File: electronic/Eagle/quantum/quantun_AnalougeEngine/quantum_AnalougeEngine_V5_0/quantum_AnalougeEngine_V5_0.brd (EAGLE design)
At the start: 200 x 80 mm, 198 parts, among them IC1 OP275, IC10 STM32F767ZIT6, IC11 AD7606BSTZ, IC12 ESDA6V1BC6, IC2 DAC084S085CIMM_NOPB, IC3 DAC084S085CIMM_NOPB, IC4 OP275, IC5 OP275, IC6 LAN8742A-CZ-TR, IC7 TL072, IC8 OP275, IC9 TL072, J1 GWLEX-SMT-S988G_Y, K1 K1, K2 K2, K3 K3, K4 K4, K5 K5, K6 K6, K7 K7, K8 K8, T1 H1102NL, U12 ULN2003, U4 THAT1240, U6 THAT1240, U7 THAT1240, U8 THAT1240

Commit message: progress Analog Engine V_5_0
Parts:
- removed ANALOGVOLT, DIG_VOLT: 90814-0204, electro_mechanical:MOLEX_90814-0204
- removed LED10, LED11, LED9: LED_BLUE_SMD, C_Sager_Bibliothek:WL-SMCW_0603
- added +12V_OK, +15V_OK, +3V3_OK, +5V_OK, -15V_OK: LED_GREEN_SMD, passive components:WL-SMCW_0603
- added ANALOG_VOLT, DIGITAL_VOLT, DISPLAY: 90814-0204, electro_mechanical:MOLEX_90814-0204
- added C100: 30 pF, passive components:C0603
- added C101: 4.7 uF, passive components:C1206
- added C102, C91, C99: 10 uF, passive components:C1206
- added C103, C95, C96, C97, C98: 100nF, C_Sager_Bibliothek:C0603
- added C65, C66: 2.7 pF, passive components:C0603
- added C69, C70: 4.3 pF, passive components:C0603
- added C71, C72: 2.2 uF, passive components:C1206
- added C73, C74, C75, C76, C77, C78, C79, C80, C81, C82, C83, C84, C85, C86, C87, C90, C92, C93, C94: 100 nF, passive components:C0603
- added C88: 1 uF, passive components:C0603
- added C89: 470 pF, passive components:C0603
- added IC13: USBLC6-4SC6, NUCLEO_parts:SOT95P280X145-6N
- added IC14, IC15: TL072, C_Sager_Bibliothek:SOIC8
- added IC16: OP275, C_Sager_Bibliothek:SOIC8
- added LD1, LD2, LD3: LED_BLUE_SMD, C_Sager_Bibliothek:WL-SMCW_0603
- added R100: 150 R, C_Sager_Bibliothek:R0603
- added R101: 500 R, C_Sager_Bibliothek:R0603
- added R20, R21, R23, R27, R85: 10 k, C_Sager_Bibliothek:R0603
- added R22: 1k5, C_Sager_Bibliothek:R0603
- added R24, R25, R26: 33 R, C_Sager_Bibliothek:R0603
- added R77: 12k1, C_Sager_Bibliothek:R0603
- added R79, R80, R81, R82: 50 R, C_Sager_Bibliothek:R0603
- added R83, R84: 270 R, C_Sager_Bibliothek:R0603
- added R86: 100k, C_Sager_Bibliothek:R0603
- added R87: 10k, C_Sager_Bibliothek:R0603
- added R88, R89, R90: 75 R, C_Sager_Bibliothek:R0603
- added R91: 0 R, C_Sager_Bibliothek:R0603
- added R97, R98: 650 R, C_Sager_Bibliothek:R0603
- added R99: 65 R, C_Sager_Bibliothek:R0603
- added Y1: NX3215SA-32.768K-STD-MUA-8, NUCLEO_parts:NX3215SA
- added Y2: NX3225GD-8MHZ-STD-CRA-3, NUCLEO_parts:RESC3226X100N
- added Y3: ABLS2-25.000MHZ-D4YF-T, NUCLEO_parts:ABLS
- C39: value 10 µF -> 10 uF; device C_Sager_Bibliothek:CAPAE400X550N -> passive components:C1206
- C40: value 10 µF -> 30 pF; device C_Sager_Bibliothek:CAPAE400X550N -> passive components:C0603
- C67: value 47µF -> 10 uF; device C_Sager_Bibliothek:CAPAE400X550N -> passive components:C1206
- C68: value 47µF -> 100nF; device C_Sager_Bibliothek:CAPAE400X550N -> C_Sager_Bibliothek:C0603
- R29: value 10k -> 75 R
- R38, R41, R44, R64: value 51k -> 27k
- R39, R45: value 51R -> 100k
- R40, R43, R63, R66: value 90k9 -> 160 k
- R42, R65: value 51R -> 10k
- moved R29 497.9 mm to (-28.8, -404.2)
- moved C40 397.1 mm to (-28.6, -304.8), turned to 0 degrees
- moved C39 393.0 mm to (-23.8, -296.6), turned to 0 degrees
- moved R65 359.0 mm to (-28.6, -329.0)
- moved R45 358.4 mm to (-28.6, -324.1)
- moved R42 357.7 mm to (-28.6, -319.2)
- moved R39 357.0 mm to (-28.6, -314.3)
- moved R59 115.8 mm to (151.6, 46.5)
- moved TP01 112.8 mm to (146.8, 43.4)
- moved R18 112.7 mm to (-25.1, -137.6)
- moved TP02 109.6 mm to (144.7, 46.6)
- moved C7 95.3 mm to (27.1, 10.1), turned to 90 degrees
- moved IC1 90.8 mm to (31.6, 10.8), turned to 90 degrees
- moved R58 89.5 mm to (127.8, 35.9)
- moved R73 89.4 mm to (127.7, 41.7)
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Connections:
- net USB_DM renamed USB_N
- net USB_DP renamed USB_P
- removed net +5V_DIGITAL: R1.2
- removed net ADC1-IN0: R3.1, R4.2
- removed net ADC1-IN3: R1.1, R2.2
- removed net DGND: C19.2, C31.2, C33.2, C43.2, IC2.6, IC3.6
- removed net EP_VSS: IC6.25
- removed net N$216: IC10.110
- removed net PB2/BOOT1: IC10.48, R18.2
- removed net RMSII_CRS_DV: IC10.43
- removed net VDD1A: IC6.19
- removed net VDD2A: IC6.1
- removed net VDDCR: IC6.6
- removed net VDDIO: IC6.9
- new net +12V_SIG: IC10.42, R39.1, R42.2
- new net +15V_SIG: IC10.34, R3.1, R4.2
- new net +3V3_SIG: IC10.47, R45.1, R65.2
- new net +5V_SIG: IC10.26, R86.1, R87.2
- new net -15V_SIG: IC10.37, R1.1, R2.2
- new net 1V_DAC_UNBUFFERD: C20.1, C64.1, IC15.5, R61.2, R68.1, R69.2
- new net 32.768KHZ_A: C66.1, IC10.8, Y1.1
- new net 32.768KHZ_B: C65.1, IC10.9, Y1.2
- new net 8MHZ_CRYSTAL_A: C70.1, IC10.23, Y2.1
- new net 8MHZ_CRYSTAL_B: C69.1, IC10.24, Y2.2
- new net LED1: IC6.3, J1.10, R85.2
- new net LED2: IC6.2, J1.12
- new net N$15: C71.1, IC10.71
- new net N$17: C72.1, IC10.106
- new net N$20: C80.2, IC10.32, IC10.33
- new net N$21: IC6.7, R18.2, R24.2
- new net N$22: IC6.8, R20.2, R25.2
- new net N$23: IC6.11, R21.2, R26.2
- new net N$24: IC6.10, R27.2
- new net N$25: IC6.24, R77.1
- new net N$27: C88.2, C89.2, IC6.6
- new net N$35: J1.1, T1.16
- new net N$36: J1.2, T1.14
- new net N$37: J1.3, T1.11
- new net N$46: J1.6, T1.9
- new net N$50: J1.11, R84.2
- new net N$52: J1.9, R83.2
- new net N$62: IC7.5, R46.2, R73.1
- new net N$66: IC14.5, R58.2, R59.1
- new net N$67: IC15.3, R60.2, R61.1
- new net N$69: C40.2, IC6.4, Y3.1
- new net N$70: C100.2, IC6.5, Y3.2
- new net N$76: -15V_OK.2, R97.2
- new net N$82: +15V_OK.2, R98.1
- new net N$83: +3V3_OK.2, R99.1
- new net N$84: +5V_OK.2, R100.1
- new net N$85: +12V_OK.2, R101.1
- new net N$86: J1.7, R29.2
- new net N$87: J1.8, R88.2
- new net N$88: R89.2, T1.12
- new net N$89: R90.2, T1.15
- new net N$90: C101.1, R29.1, R88.1, R89.1, R90.1
- new net N$92: C101.2, J1.MP1, J1.MP2, R91.2
- new net RD_N: IC13.6, IC6.22, R82.1, T1.8
- new net RD_P: IC13.1, IC6.23, R81.1, T1.6
- new net RMII_CRS_DV: IC10.43, R26.1
- new net TD_N: IC13.4, IC6.20, R80.1, T1.3
- new net TD_P: IC13.3, IC6.21, R79.1, T1.1
- new net USB_OVERCURRENT: IC10.92
- new net USB_POWERSWITCHON: IC10.91
- new net USB_SOF: IC10.100
- net +12V: now also DIGITAL_VOLT.2, DISPLAY.3, R101.2, R39.2; no longer ANALOGVOLT.2
- net +3V3: now also C73.1, C74.1, C75.1, C76.1, C77.1, C78.1, C79.1, C81.2, C82.2, C83.1, C84.1, C85.1, C86.2, C87.2, C90.2, C91.1, C92.2, C93.2, C94.2, DIGITAL_VOLT.1, IC10.108, IC10.121, IC10.131, IC10.144, IC10.17, IC10.30, IC10.39, IC10.52, IC10.6, IC10.62, IC10.72, IC10.84, IC10.95, IC13.5, IC6.1, IC6.19, IC6.9, R18.1, R20.1, R21.1, R22.1, R23.2, R45.2, R79.2, R80.2, R81.2, R82.2, R99.2, T1.2, T1.7; no longer ANALOGVOLT.1
- net +5V: now also C24.1, C34.1, DIGITAL_VOLT.4, IC2.7, R1.2, R100.2, R86.2; no longer ANALOGVOLT.4, R29.2
- net .: now also IC14.1; no longer IC7.7
- net 0,5V_DAC: now also IC14.3, IC15.1, IC15.2; no longer IC7.5, R60.2, R61.1
- net 1V_DAC: now also IC15.6, IC15.7; no longer C20.1, C24.1, C34.1, C64.1, IC2.7, R61.2, R68.1, R69.2
- net AGND: now also +12V_OK.1, +15V_OK.1, +3V3_OK.1, +5V_OK.1, -15V_OK.1, C100.1, C103.2, C19.2, C31.2, C33.2, C40.1, C43.2, C65.2, C66.2, C68.2, C69.2, C70.2, C71.2, C72.2, C73.2, C74.2, C75.2, C76.2, C77.2, C78.2, C79.2, C80.1, C81.1, C82.1, C83.2, C84.2, C85.2, C86.1, C87.1, C88.1, C89.1, C90.1, C91.2, C92.1, C93.1, C94.1, C95.2, C96.2, C97.2, C98.2, C99.2, DISPLAY.4, IC10.107, IC10.120, IC10.130, IC10.16, IC10.31, IC10.38, IC10.51, IC10.61, IC10.83, IC10.94, IC13.2, IC2.6, IC3.6, IC6.25, R27.1, R77.2, R83.1, R84.1, R85.1, R87.1; no longer C40.2, R18.1, R39.1, R45.1
- net A_GND_TO_STAR: now also ANALOG_VOLT.3; no longer DIG_VOLT.3
- net CHASIS: now also R91.1
- net DAC2_OUT1(OFFSET_VCA1): now also C99.1; no longer C39.1
- net DAC2_OUT2(OFFSET_VCA2): now also C39.1; no longer C40.1
- net D_GND_TO_STAR: now also DIGITAL_VOLT.3; no longer ANALOGVOLT.3
- net E+_OUT_STAGE_LEFT: now also IC7.6, IC7.7; no longer R46.2, R73.1
- net E+_OUT_STAGE_RIGHT: now also IC14.6, IC14.7; no longer R58.2, R59.1
- net L/M_IN(VCA1_IN): now also C102.1; no longer C67.1
- net LD1: now also LD1.2; no longer LED9.2
- net LD2: now also LD2.2; no longer LED10.2
- net LD3: now also LD3.2; no longer LED11.2
- net N$12: now also LD2.1; no longer LED10.1
- net N$18: now also U6.3; no longer U6.2
- net N$33: now also IC16.1, IC16.2, U6.2; no longer IC4.6, IC4.7, U6.3
- net N$34: now also LD3.1; no longer LED11.1
- net N$38: no longer R29.1
- net N$43: now also U8.2; no longer U8.3
- net N$45: now also U8.3; no longer U8.2
- net N$6: now also LD1.1; no longer LED9.1
- net N$71: now also C102.2; no longer C67.2
- net N$74: now also IC14.2; no longer IC7.6
- net N$78: now also C67.2; no longer C68.2
- net NRST: now also IC6.15
- net R: now also IC16.3; no longer IC4.5
- net R/S_IN(VCA2_IN): now also C67.1; no longer C68.1
- net RMII_MDC: now also IC6.13
- net RMII_MDIO: now also IC6.12, R22.2
- net RMII_REF_CLK: now also IC6.14, R23.1
- net RMII_RXD0: now also R25.1
- net RMII_RXD1: now also R24.1
- net RMII_TXD0: now also IC6.17
- net RMII_TXD1: now also IC6.18
- net RMII_TX_EN: now also IC6.16
- net SYM1: no longer R39.2
- net SYM2: no longer R42.2
- net SYM3: no longer R45.2
- net SYM4: no longer R65.2
- net USART6_RX: now also DISPLAY.2, IC10.97; no longer IC10.96
- net USART6_TX: now also DISPLAY.1, IC10.96; no longer IC10.97
- net V+: now also ANALOG_VOLT.1, C68.1, C95.1, C97.1, IC14.8, IC15.8, IC16.8, R98.2; no longer DIG_VOLT.1
- net V-: now also ANALOG_VOLT.2, C103.1, C96.1, C98.1, IC14.4, IC15.4, IC16.4, R97.1; no longer DIG_VOLT.2
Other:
- board size 200 x 80 mm -> 210 x 70 mm

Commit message: progress on Analog Engine_v5_0
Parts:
- moved Y3 398.8 mm to (171.6, 50.6)
- moved C98 365.8 mm to (109.2, 49.7), turned to 180 degrees
- moved C97 353.5 mm to (105.3, 42.6)
- moved IC15 351.2 mm to (107.3, 46.2), turned to 90 degrees
- moved C96 334.1 mm to (109.1, 31.8)
- moved C95 322.0 mm to (105.0, 24.9)
- moved IC14 313.0 mm to (107.1, 28.4), turned to 90 degrees
- moved IC13 277.9 mm to (192.3, 50.4)
- moved DEBUG2 160.7 mm to (156.9, 5.90), turned to 90 degrees
- moved DEBUG1 157.9 mm to (154.4, 5.90), turned to 90 degrees
- moved TP04 157.8 mm to (153.0, 19.4)
- moved LED4 141.2 mm to (171.3, 14.0)
- moved R15 89.3 mm to (87.7, 2.90)
- moved IC5 72.1 mm to (47.9, 11.0)
- moved C35 72.1 mm to (53.1, 12.9)
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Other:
- board text added: "LD1"
- board text added: "LD2"
- board text added: "LD3"

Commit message: placement of components done AnalougeEngine V5_0
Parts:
- added R92, R93, R94, R95: 500 R, C_Sager_Bibliothek:R0603
- moved R91 521.4 mm to (203.0, 43.2), turned to 180 degrees
- moved R90 520.5 mm to (197.8, 49.7), turned to 90 degrees
- moved R89 517.0 mm to (199.9, 49.7), turned to 90 degrees
- moved R88 514.5 mm to (204.1, 49.7), turned to 90 degrees
- moved R29 509.2 mm to (202.0, 49.7), turned to 90 degrees
- moved C101 498.2 mm to (199.1, 43.2)
- moved R101 482.4 mm to (207.2, 23.9)
- moved +12V_OK 468.7 mm to (204.1, 23.9)
- moved R100 468.7 mm to (207.2, 13.1)
- moved R99 466.9 mm to (207.2, 15.9)
- moved +15V_OK 457.0 mm to (204.1, 18.7)
- moved +5V_OK 457.0 mm to (204.1, 13.1)
- moved -15V_OK 457.0 mm to (204.1, 21.5)
- moved +3V3_OK 457.0 mm to (204.1, 15.9)
- moved R98 453.2 mm to (207.2, 18.8), turned to 180 degrees
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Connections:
- new net N$91: IC2.10, IC3.10, R92.1
- new net N$93: IC2.8, IC3.8, R93.1
- new net N$94: IC2.9, R94.1
- new net N$95: IC3.9, R95.1
- net CS_DAC1: now also R94.2; no longer IC2.9
- net CS_DAC2: now also R95.2; no longer IC3.9
- net DIN_DAC: now also R93.2; no longer IC2.8, IC3.8
- net SCLK_DAC: now also R92.2; no longer IC2.10, IC3.10
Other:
- board text removed: "AGND"

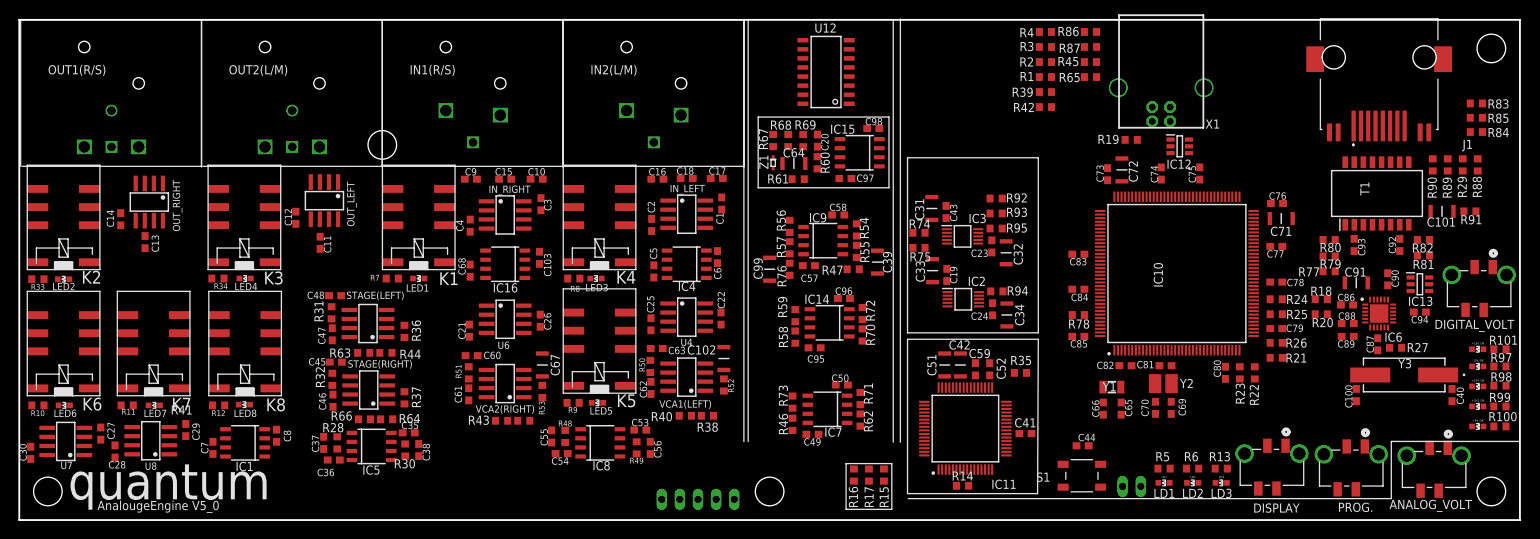
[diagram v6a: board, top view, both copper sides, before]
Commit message: Clock changed to 8 MHz Crystal. Progress AnalougeEngine (routing 50 %).
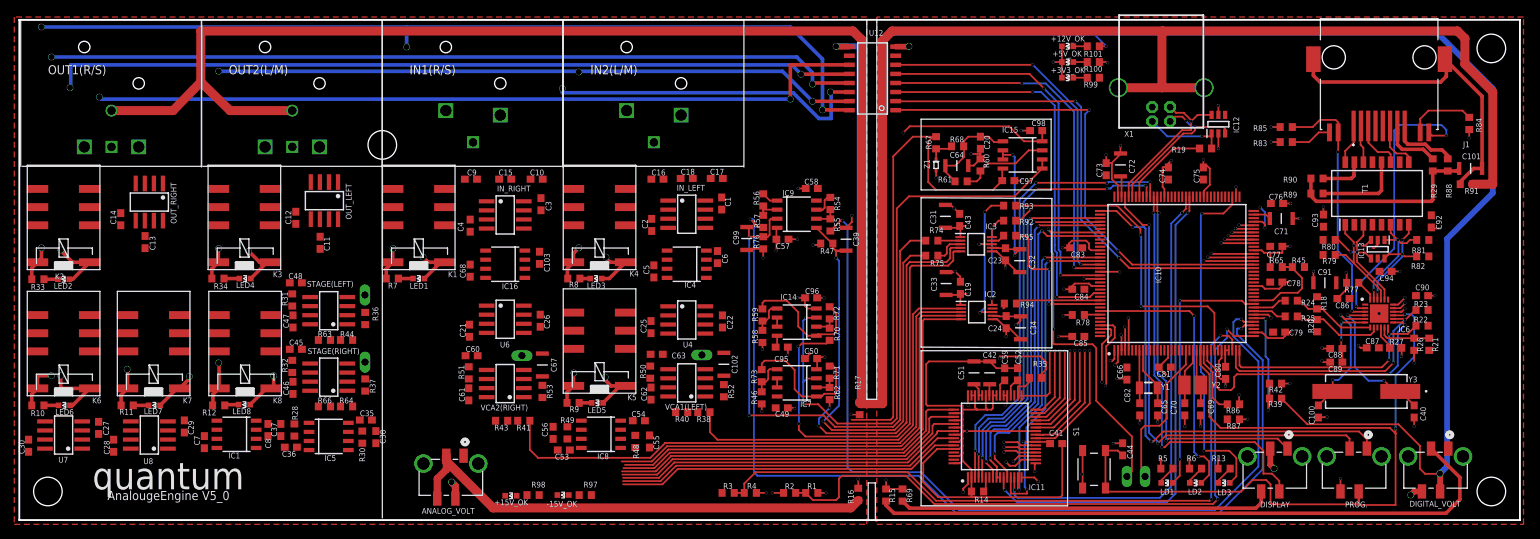
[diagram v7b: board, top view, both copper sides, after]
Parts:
- removed TP04: TPTHT, C_Sager_Bibliothek:THT_PIN
- R68: value 10k -> 20k
- R69: value 10k -> 0R
- moved ANALOG_VOLT 137.6 mm to (62.3, 9.00)
- moved +15V_OK 136.2 mm to (68.8, 3.40)
- moved R98 136.2 mm to (71.9, 3.50)
- moved -15V_OK 129.3 mm to (76.1, 3.50)
- moved R97 129.3 mm to (79.2, 3.50)
- moved +5V_OK 76.8 mm to (146.7, 64.1)
- moved R4 76.6 mm to (102.3, 3.80)
- moved R3 76.6 mm to (99.2, 3.80), turned to 180 degrees
- moved R100 76.4 mm to (150.3, 64.1)
- moved +3V3_OK 73.6 mm to (146.7, 61.9)
- moved R99 73.2 mm to (150.3, 61.9)
- moved +12V_OK 71.4 mm to (146.7, 66.3)
- moved R101 71.0 mm to (150.3, 66.3)
- moved R2 70.1 mm to (107.8, 3.80), turned to 0 degrees
- moved R1 66.8 mm to (110.9, 3.80)
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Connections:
- new net DISPLAY_GND_TO_STAR: DISPLAY.4, R69.1
- net +12V: no longer DISPLAY.3
- net +5V: now also DISPLAY.3
- net 1V_DAC_UNBUFFERD: no longer R69.2
- net AGND: now also R69.2; no longer DISPLAY.4, R69.1
- net A_GND_TO_STAR: now also ANALOG_VOLT.4
- net CHASIS: now also X1.P$1, X1.P$2; no longer TP04.P$1
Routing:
- net +12V: track 0.00 -> 649.8 mm, vias 0 -> 11
- net CHASIS: track 0.00 -> 361.1 mm
- net AGND: track 0.00 -> 283.0 mm, vias 0 -> 73
- net OUT1_DRIVER: track 0.00 -> 194.3 mm, vias 0 -> 5
- net OUT6_DRIVER: track 0.00 -> 170.1 mm, vias 0 -> 3
- net OUT5_DRIVER: track 0.00 -> 165.6 mm, vias 0 -> 3
- net OUT4_DRIVER: track 0.00 -> 165.3 mm, vias 0 -> 3
- net OUT2_DRIVER: track 0.00 -> 149.1 mm, vias 0 -> 5
- net DAC_OUT1: track 0.00 -> 137.9 mm, vias 0 -> 2
- net DAC_OUT2: track 0.00 -> 124.4 mm, vias 0 -> 2
- net NRST: track 0.00 -> 123.5 mm, vias 0 -> 2
- net +15V_SIG: track 0.00 -> 97.3 mm, vias 0 -> 2
- net -15V_SIG: track 0.00 -> 93.1 mm, vias 0 -> 2
- net OUT3_DRIVER: track 0.00 -> 91.2 mm, vias 0 -> 3
- net D_GND_TO_STAR: track 0.00 -> 90.9 mm
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- added copper zone on layer 1, net +3V3
- added copper zone on layer 15, net +5V
- added copper zone on layer 2, net AGND
- added copper zone on layer 1, net V+
- added copper zone on layer 15, net V-
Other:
- board text removed: "LD1"
- board text removed: "LD2"
- board text removed: "LD3"

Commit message: Analouge Engine V5_0 updates...
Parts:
- removed C103: 100nF, C_Sager_Bibliothek:C0603
- added C104: 100 nF, passive components:C0603
- C1, C11, C12, C13, C14, C19, C2, C20, C21, C22, C23, C24, C25, C26, C27, C28, C29, C3, C30, C35, C36, C4, C43, C44, C45, C46, C47, C48, C49, C5, C50, C53, C54, C57, C58, C6, C60, C61, C62, C63, C68, C7, C8, C95, C96, C97, C98: value 100nF -> 100 nF; device C_Sager_Bibliothek:C0603 -> passive components:C0603
- C10, C15, C16, C17, C18, C9: device C_Sager_Bibliothek:C0603 -> passive components:C0603
- C37, C38, C55, C56: value 22pF -> 22 pF; device C_Sager_Bibliothek:C0603 -> passive components:C0603
- moved C14 117.9 mm to (131.7, 32.5)
- moved C36 98.9 mm to (131.6, 42.0), turned to 90 degrees
- moved C43 94.6 mm to (38.7, 23.9), turned to 0 degrees
- moved C6 76.2 mm to (25.9, 11.3), turned to 90 degrees
- moved C20 75.9 mm to (63.1, 27.1), turned to 90 degrees
- moved C48 70.2 mm to (106.7, 15.7)
- moved C26 63.5 mm to (11.2, 13.0)
- moved C58 52.9 mm to (63.4, 23.1), turned to 0 degrees
- moved C23 50.7 mm to (88.4, 26.6), turned to 90 degrees
- moved C30 47.3 mm to (48.5, 14.0), turned to 0 degrees
- moved C22 40.6 mm to (138.0, 36.9)
- moved C54 40.6 mm to (110.7, 46.6), turned to 180 degrees
- moved C50 36.8 mm to (76.3, 9.70)
- moved C21 35.3 mm to (98.3, 27.6), turned to 270 degrees
- moved C63 28.5 mm to (63.2, 34.8), turned to 90 degrees
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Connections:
- net +5V: now also C14.1, C36.1; no longer C19.1, C43.1
- net 1V_DAC: now also C22.1; no longer C23.1
- net 1V_DAC_UNBUFFERD: now also C19.1; no longer C20.1
- net AGND: now also C104.2; no longer C103.2
- net L/M_OUT(OUT_STAGE_LEFT): now also C38.2; no longer C37.2
- net N$48: now also C38.1; no longer C37.1
- net N$53: now also C37.1; no longer C38.1
- net N$54: now also C43.1; no longer C45.1
- net N$73: now also C47.1; no longer C48.1
- net N$77: now also C58.1; no longer C60.1
- net N$80: now also C61.1; no longer C63.1
- net R/S_OUT(OUT_STAGE_RIGHT): now also C37.2; no longer C38.2
- net V+: now also C104.1, C12.1, C21.1, C25.1, C27.1, C29.1, C4.1, C45.1, C48.1, C50.1, C54.1, C6.1, C60.1, C63.1, C8.1; no longer C1.1, C11.1, C13.1, C22.1, C26.1, C28.1, C35.1, C47.1, C49.1, C5.1, C53.1, C58.1, C61.1, C68.1, C7.1
- net V-: now also C1.1, C11.1, C13.1, C20.1, C23.1, C26.1, C28.1, C35.1, C49.1, C5.1, C53.1, C68.1, C7.1; no longer C103.1, C12.1, C14.1, C21.1, C25.1, C27.1, C29.1, C36.1, C4.1, C50.1, C54.1, C6.1, C8.1
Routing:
- net EC+_VCA2(RIGHT): track 3.28 -> 71.8 mm, vias 0 -> 2
- net AGND: track 283.0 -> 329.5 mm, vias 73 -> 96
- net CHASIS: track 361.1 -> 405.7 mm
- net N$18: track 0.00 -> 38.5 mm, vias 0 -> 3
- net N$33: track 0.00 -> 38.3 mm, vias 0 -> 2
- net EC+_VCA1(LFT): track 2.34 -> 39.0 mm, vias 0 -> 2
- net N$2: track 0.00 -> 35.0 mm, vias 0 -> 2
- net L: track 0.00 -> 34.1 mm
- net N$7: track 0.00 -> 34.1 mm, vias 0 -> 2
- net R: track 0.00 -> 33.3 mm
- net V-: track 82.2 -> 111.2 mm, vias 6 -> 14
- net POSITIVE_IN(R/S): track 0.00 -> 25.6 mm
- net POSITIVE_IN(L/M): track 0.00 -> 24.0 mm
- net V+: track 71.4 -> 94.4 mm
- net NEGATIVE_IN(R/S): track 0.00 -> 18.8 mm
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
